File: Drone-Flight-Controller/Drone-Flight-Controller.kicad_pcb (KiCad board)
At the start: 4 copper layers, 30 x 65 mm, 60 parts, among them J1 Screw_Terminal_01x02, J10 TestPoint, J2 Raspberry_Pi_4, J3 USB_B_Micro, J4 Conn_ARM_SWD_TagConnect_TC203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, J5 TestPoint, J6 TestPoint, J7 TestPoint, J8 TestPoint, J9 TestPoint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

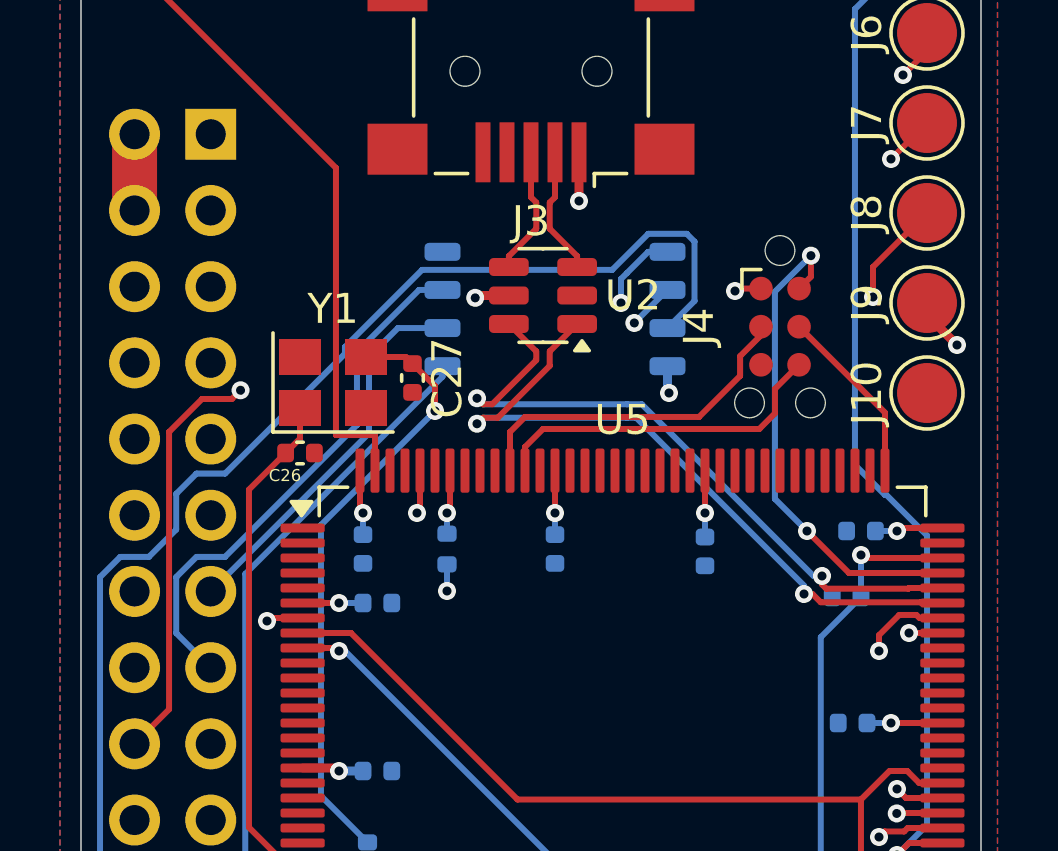
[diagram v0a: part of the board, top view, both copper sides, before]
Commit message: remove third and fourth layer traces
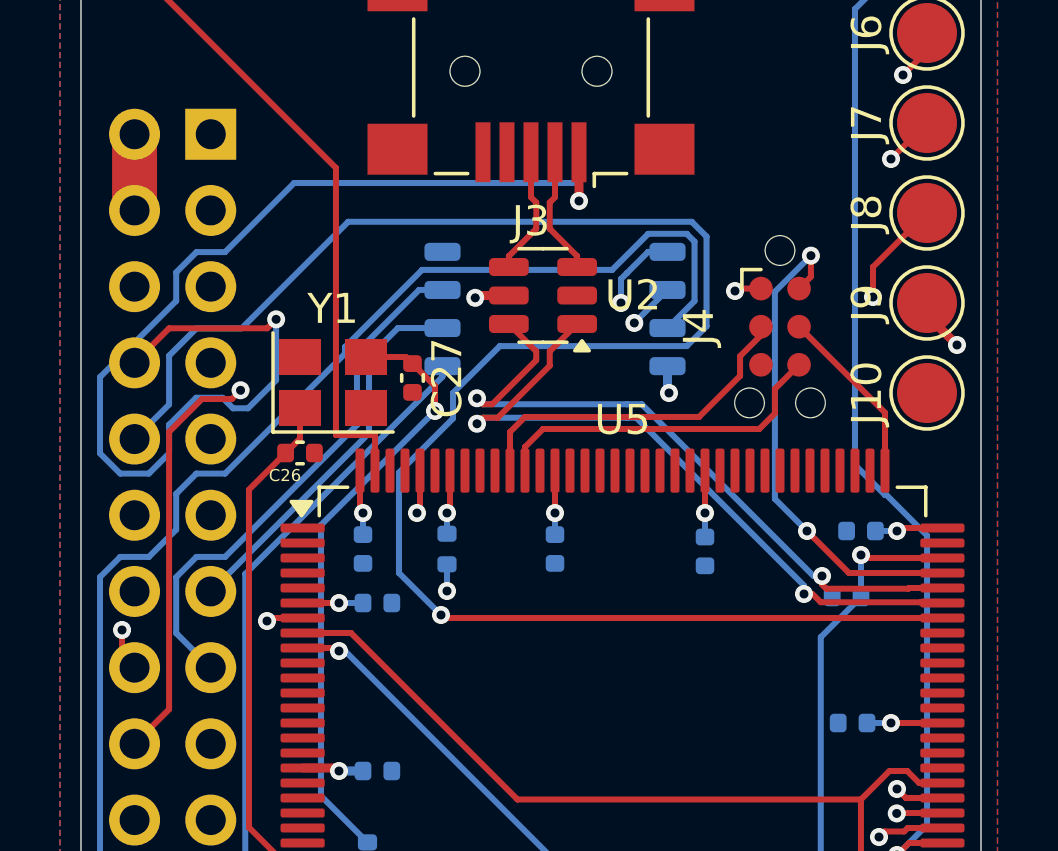
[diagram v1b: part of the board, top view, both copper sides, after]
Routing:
- net UART_RX: track 30.7 -> 61.1 mm
- net UART_TX: track 30.7 -> 37.2 mm
- net SD_CARD_CMD: vias 1 -> 2
